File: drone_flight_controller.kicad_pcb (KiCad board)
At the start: 4 copper layers, 33.5 x 33.5 mm, 70 parts, among them J1 Conn_01x08_MountingPin, J2 USB_C_Receptacle_USB2.0_16P, J3 Conn_01x06_MountingPin, U1 STM32H743VITx, U2 IST8310, U3 BMP388, U4 ICM-42688-P, U5 LT3045xDD, U6 LM5164DDA, Y1 25MHz, Y2 32.768KHz

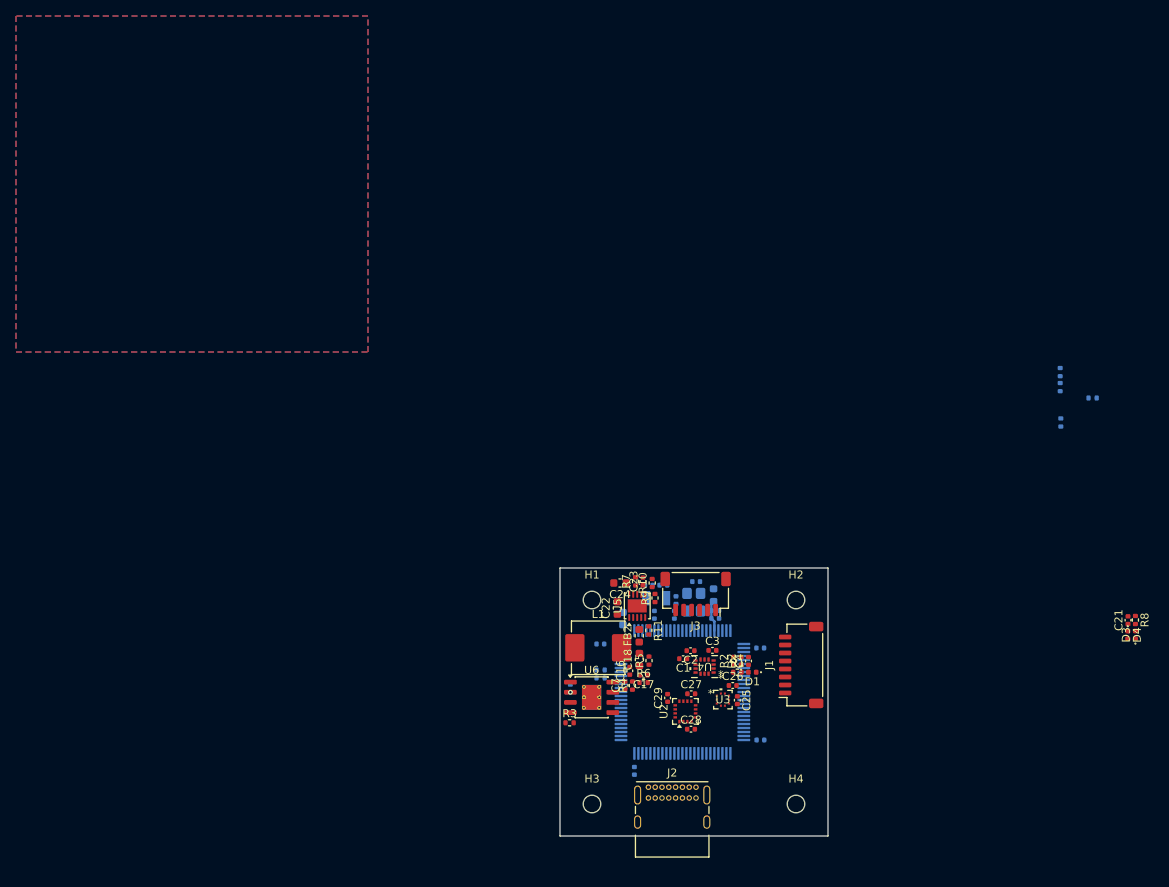
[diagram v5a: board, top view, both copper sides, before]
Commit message: added most routing, still needs to be cleaned up
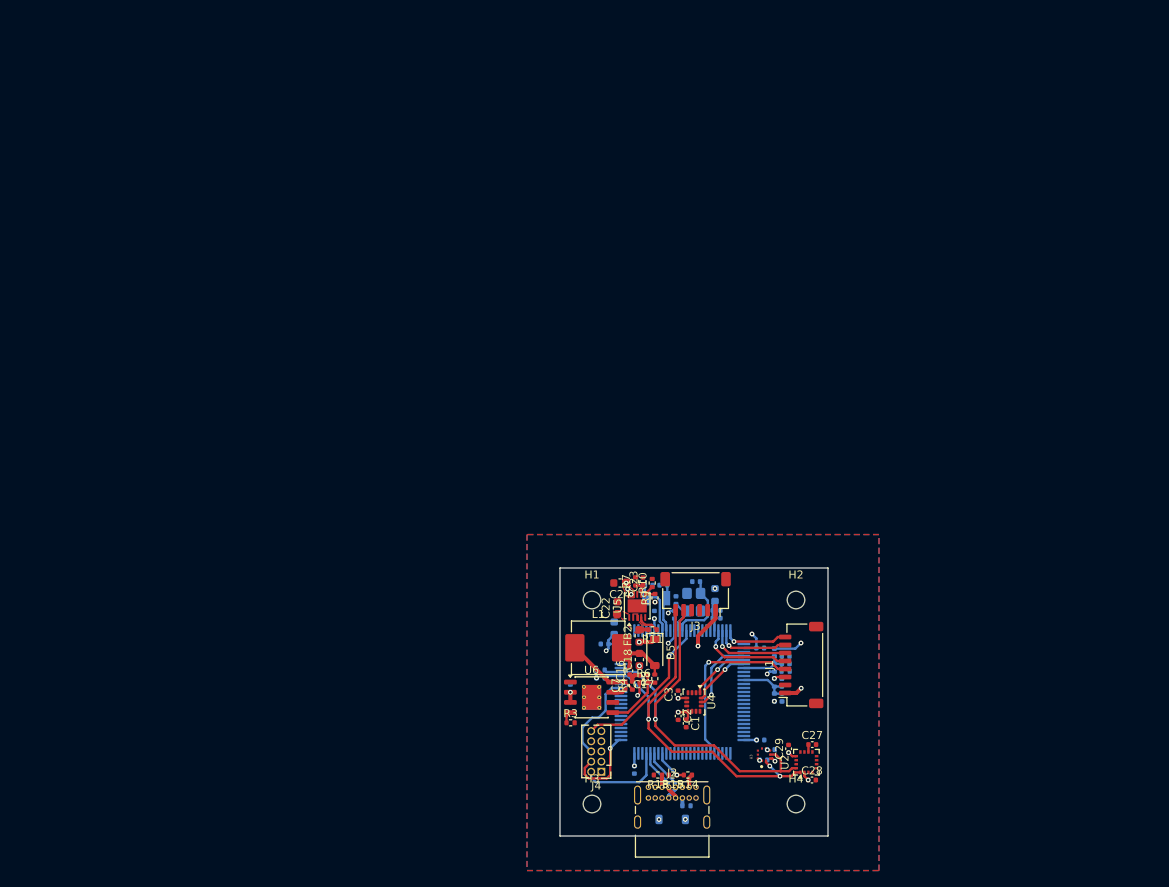
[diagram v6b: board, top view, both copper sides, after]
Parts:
- added D5: D_Schottky, Diode_SMD:D_SOD-123, F.Cu at (107.8, 106.5)
- added D6: D_Schottky, Diode_SMD:D_SOD-123, B.Cu at (110.0, 127.4)
- added J4: Conn_ARM_JTAG_SWD_10, Connector_PinHeader_1.27mm:PinHeader_2x05_P1.27mm_Vertical, F.Cu at (101.2, 121.5)
- C21, C25, C26, C4, D1, D2, D3, D4, R1, R2, R8: moved to B.Cu
- R13, R14, R15: moved to F.Cu
- U3: footprint drone:QFN_BMP388_BOS -> drone:XDCR_BMP388
- U4: footprint drone:LGA14_2P5X3X0P91_TDK -> Package_LGA:LGA-14_3x2.5mm_P0.5mm_LayoutBorder3x4y
- moved R12 71.9 mm to (111.8, 125.7)
- moved R15 69.9 mm to (110.1, 121.9), turned to 180 degrees
- moved R14 67.2 mm to (112.0, 121.9), turned to 180 degrees
- moved R13 66.9 mm to (108.2, 121.9), turned to 180 degrees
- moved D3 45.8 mm to (122.8, 112.2)
- moved R8 45.8 mm to (122.8, 110.3)
- moved C21 44.0 mm to (123.7, 110.3)
- moved D4 43.9 mm to (123.8, 112.2)
- moved C27 16.4 mm to (127.5, 118.1)
- moved C28 16.4 mm to (127.5, 122.5)
- moved C29 16.4 mm to (124.6, 118.6)
- moved U2 16.4 mm to (126.8, 120.3)
- moved C26 10.1 mm to (121.4, 120.0)
- moved U3 8.58 mm to (121.5, 119.3), turned to 90 degrees
- moved C2 8.31 mm to (110.8, 114.5), turned to -90 degrees
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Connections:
- C16 pad 2: +5V -> /BUCK_OUT
- C18 pad 2: +5V -> /BUCK_OUT
- L1 pad 2: +5V -> /BUCK_OUT
- R5 pad 2: +5V -> /BUCK_OUT
- U1 pad 14: unconnected-(U1-NRST-Pad14) -> /STM32_NRST
- U1 pad 72: unconnected-(U1-PA13-Pad72) -> /SWDIO
- U1 pad 76: unconnected-(U1-PA14-Pad76) -> /SWCLK
- U1 pad 89: unconnected-(U1-PB3-Pad89) -> /SWO
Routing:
- net +BATT: track 0.00 -> 59.3 mm, vias 1 -> 3
- net /I2C_SDA: track 0.00 -> 50.0 mm, vias 0 -> 1
- net /I2C_SCL: track 0.00 -> 49.9 mm, vias 0 -> 3
- net +5V: track 0.00 -> 45.8 mm, vias 0 -> 3
- net +3.3V: track 0.00 -> 27.3 mm, vias 0 -> 20
- net /ESC_TELEM: track 0.00 -> 21.8 mm, vias 0 -> 1
- net /STM32_NRST: track 0.00 -> 19.3 mm, vias 0 -> 1
- net /USB_VBUS: track 0.00 -> 11.8 mm, vias 0 -> 1
- net /MOT_1: track 0.00 -> 11.7 mm, vias 0 -> 1
- net /SWO: track 0.00 -> 11.5 mm
- net /SWDIO: track 0.00 -> 10.9 mm
- net /SWCLK: track 0.00 -> 10.6 mm, vias 0 -> 1
- net /MOT_2: track 0.00 -> 10.2 mm, vias 0 -> 1
- net /SPI_CLK: track 0.00 -> 9.66 mm, vias 0 -> 1
- net /BUCK_SW: track 0.00 -> 9.47 mm
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- added copper zone on F.Cu, net +3.3V
- added copper zone on F.Cu, net /LDO_IN

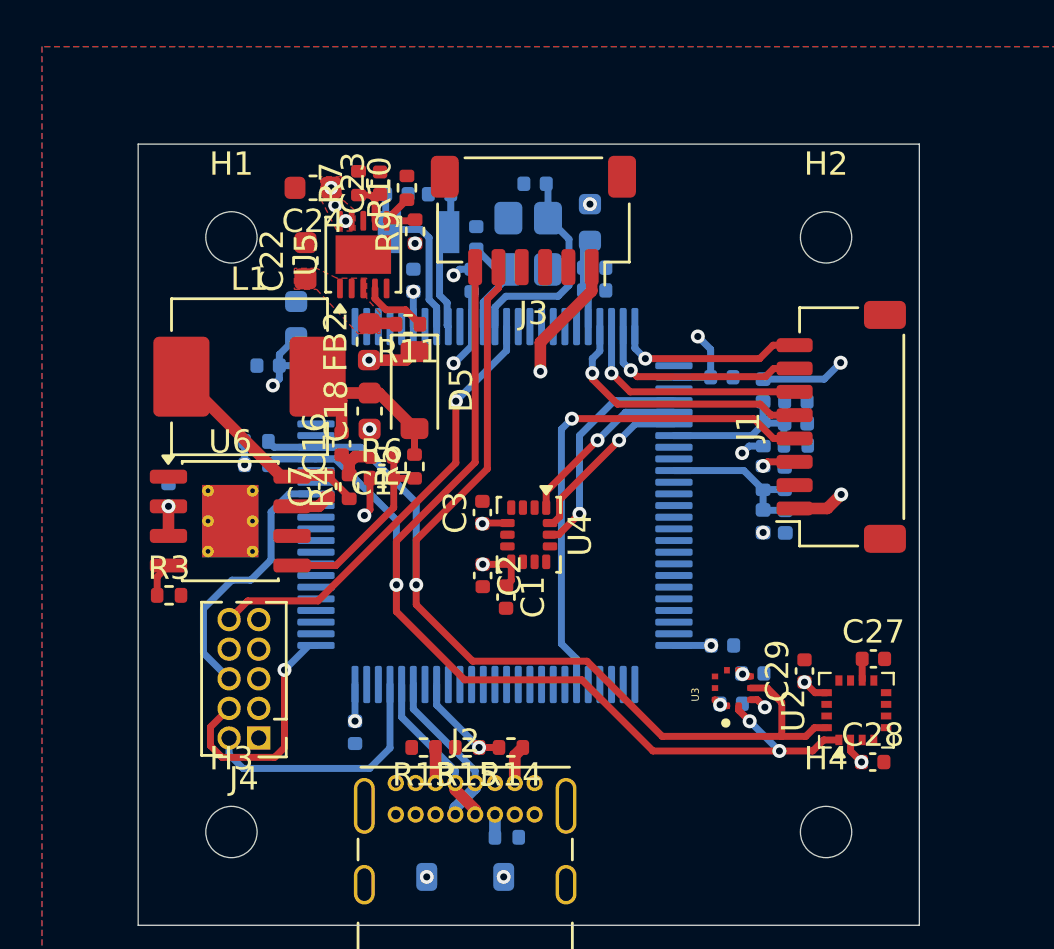
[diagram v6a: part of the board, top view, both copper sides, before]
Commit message: removed most drc violations
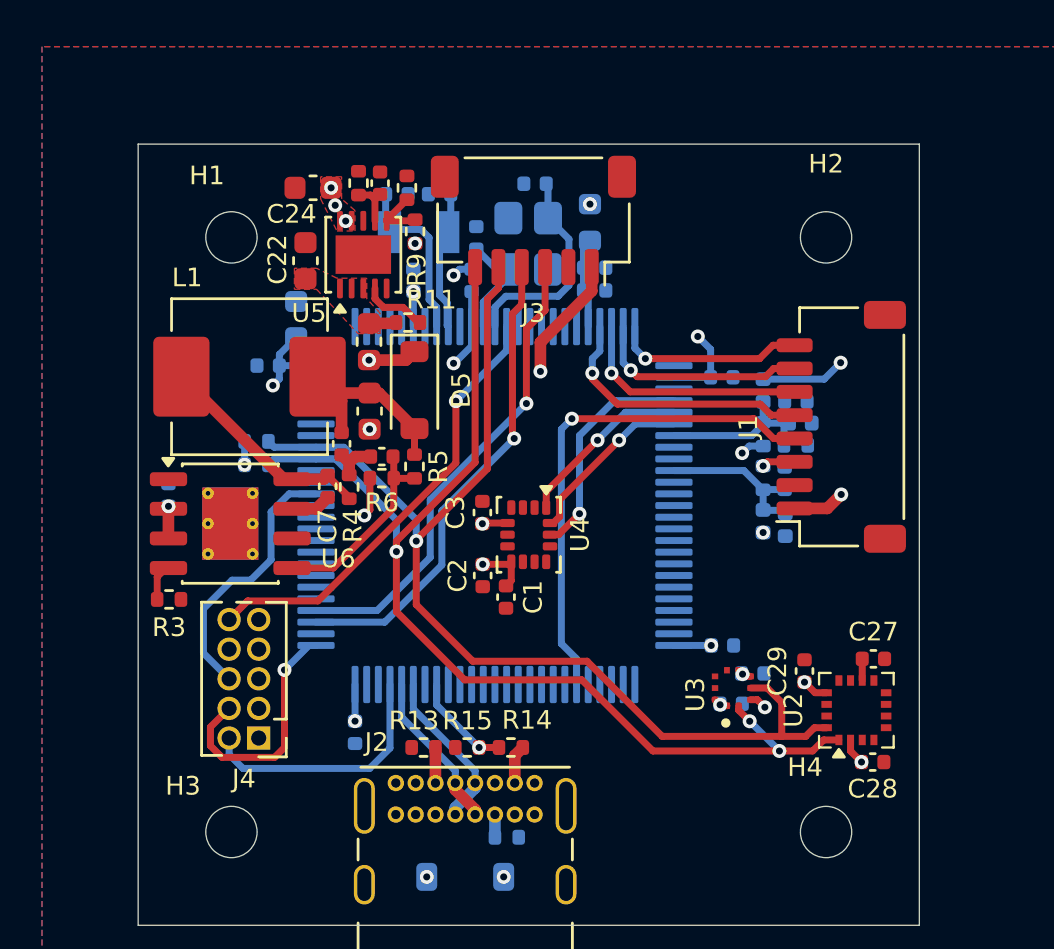
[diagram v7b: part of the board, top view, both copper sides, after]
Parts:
- moved D2 0.20 mm to (124.4, 108.0)
- moved R3 0.18 mm to (97.3, 115.5)
- moved D4 0.14 mm to (123.8, 112.3)
- moved U6 0.11 mm to (100.0, 112.3)
- moved R11 0.07 mm to (107.6, 103.7)
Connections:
- U1 pad 78: unconnected-(U1-PC10-Pad78) -> /GPS_TX
- U1 pad 79: unconnected-(U1-PC11-Pad79) -> /GPS_RX
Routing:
- net /GPS_TX: track 0.00 -> 20.7 mm, vias 0 -> 1
- net /GPS_RX: track 0.00 -> 20.3 mm, vias 0 -> 1
- net /I2C_SDA: track 50.0 -> 47.7 mm
- net /I2C_SCL: track 49.9 -> 48.5 mm
- net /VBAT_REF: track 7.83 -> 8.40 mm
